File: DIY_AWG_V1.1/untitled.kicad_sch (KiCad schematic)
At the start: 61 parts, among them U1 AMS1117-3.3, U2 ADP7118ARDZ-3.3-R7, U3 ADP7118ARDZ-3.3-R7, U4 TPS7A3301RGWR, U5 TPS7A4701RGWR, U6 TPS7A3301RGWR, U7 TPS7A4701RGWR

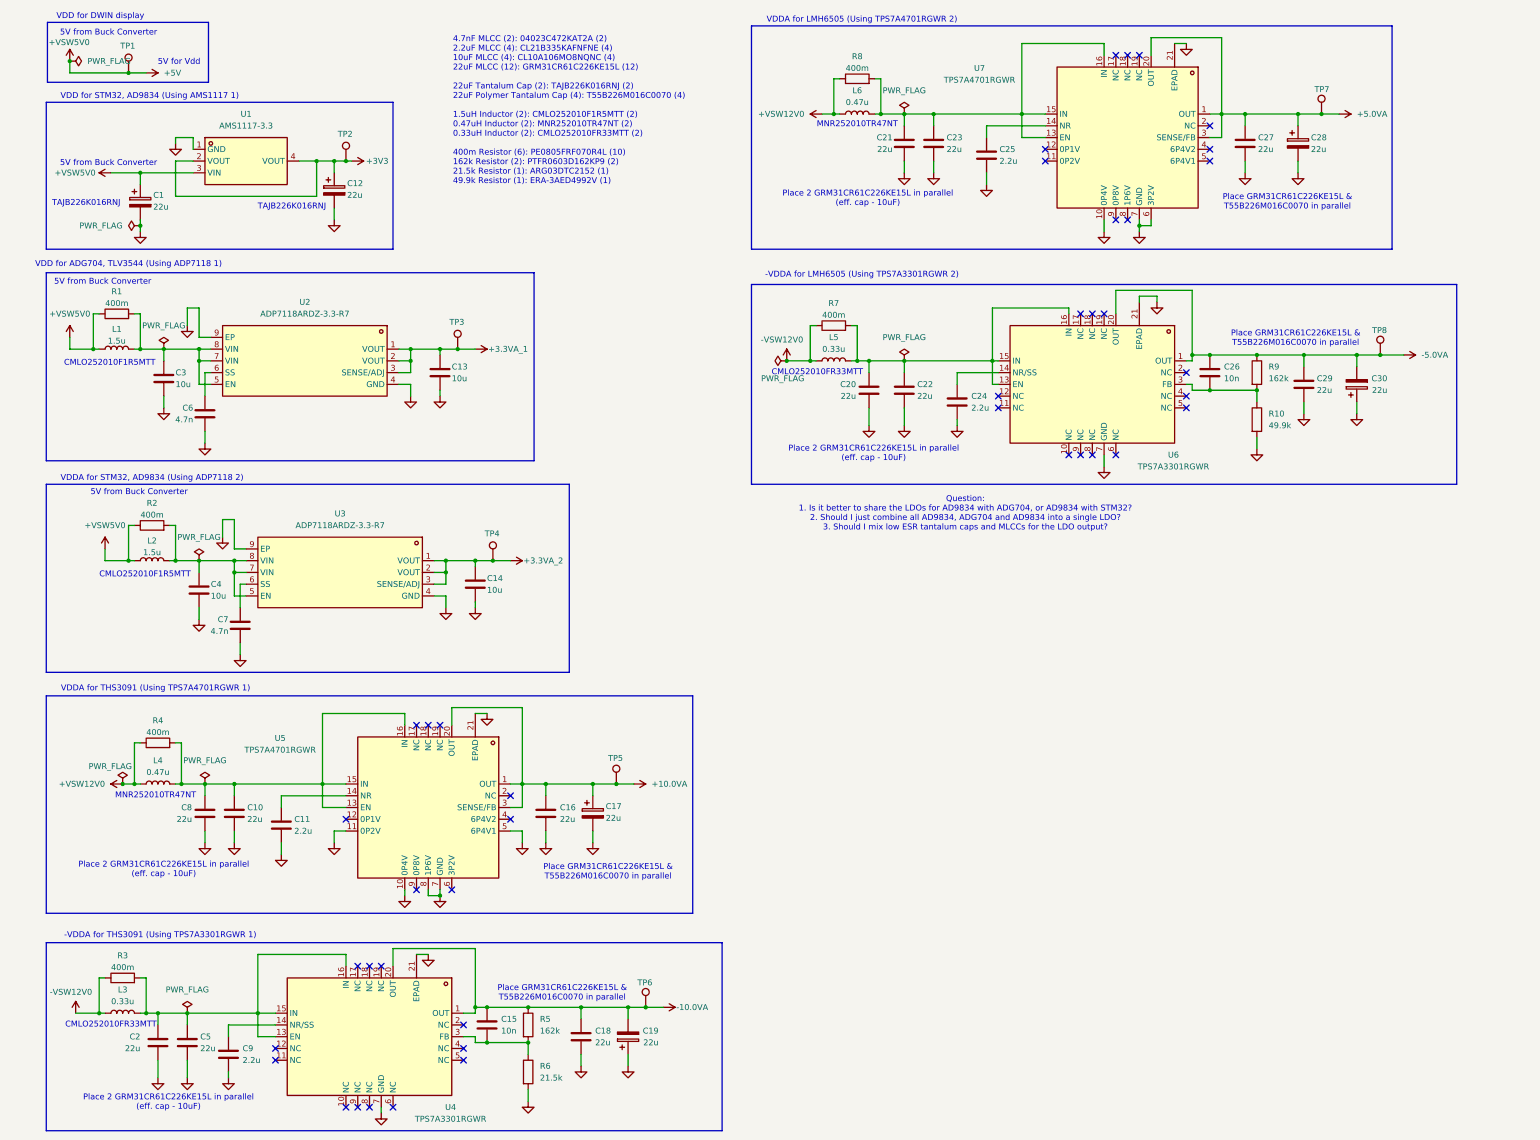
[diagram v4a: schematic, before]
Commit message: Updated component footprints
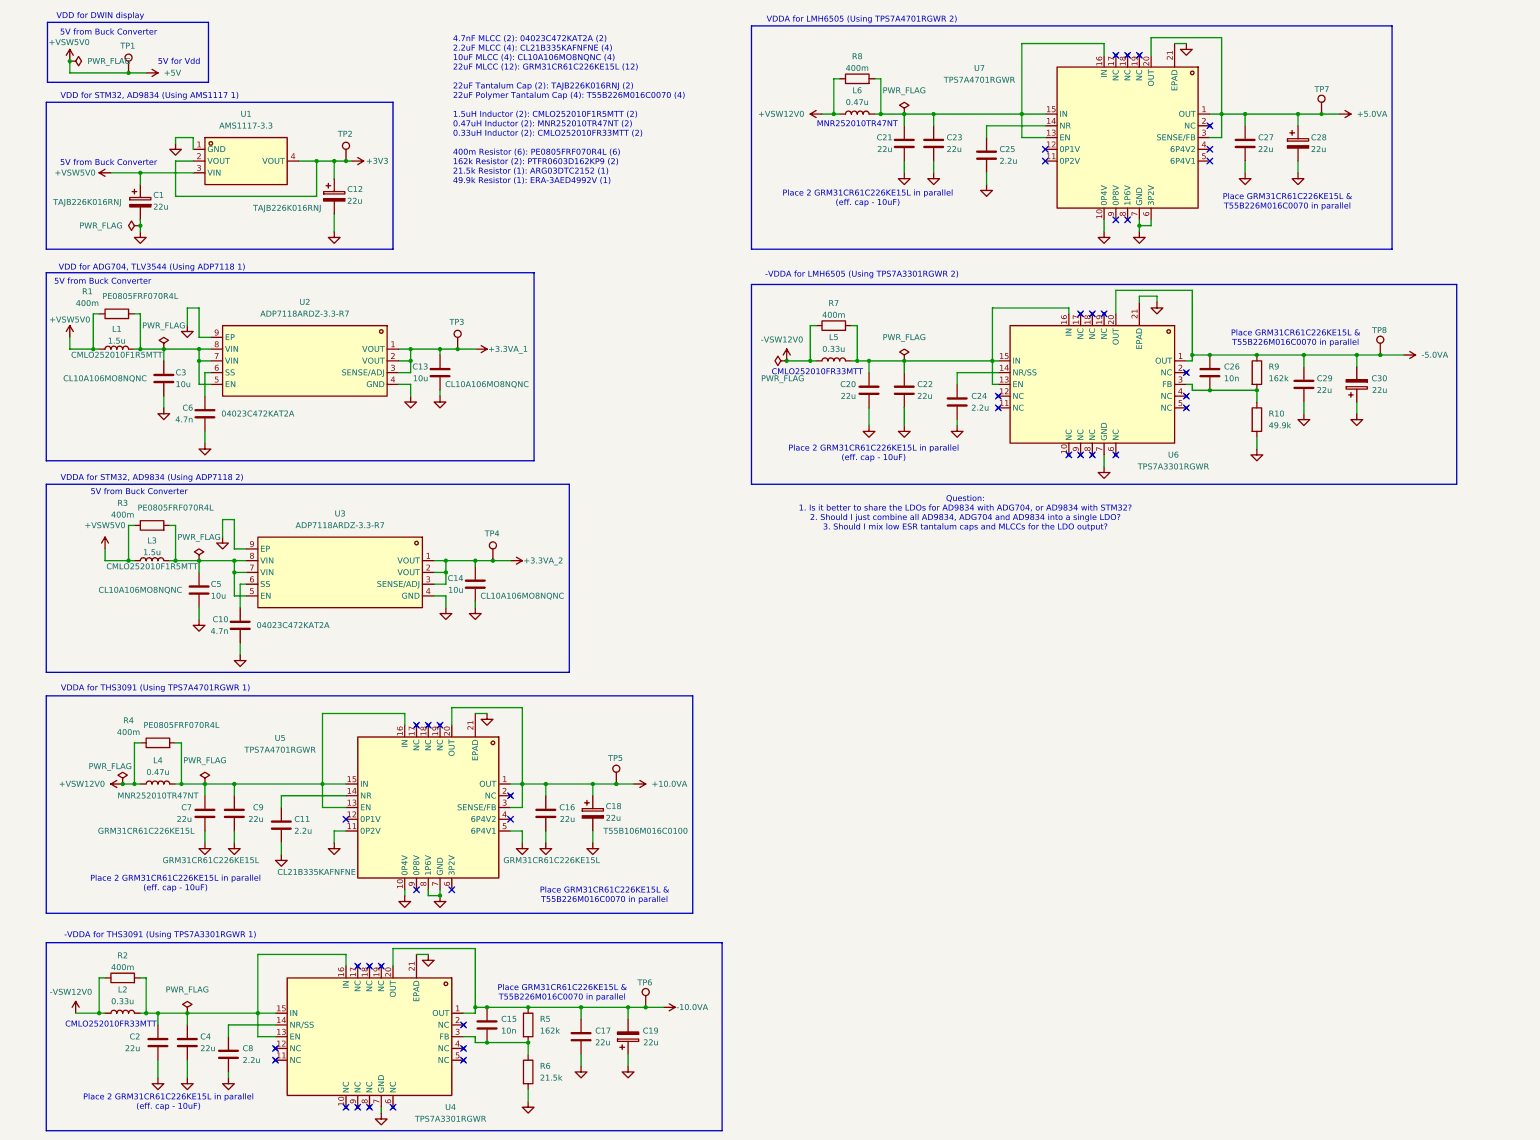
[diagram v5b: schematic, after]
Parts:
- removed C4: 10u, symbol Device:C
- removed C7: 4.7n, symbol Device:C
- removed L2: 1.5u, symbol Device:L
- removed R2: 400m, symbol Device:R
- added C5: 10u, Capacitor_SMD:C_0603_1608Metric, symbol Device:C
- added C9: 22u, Capacitor_SMD:C_1206_3216Metric, symbol Device:C
- added L3: 1.5u, Inductor_SMD:L_1008_2520Metric, symbol Device:L
- added R3: 400m, Resistor_SMD:R_0805_2012Metric, symbol Device:R
- C1: footprint (none) -> easyeda2kicad:CASE-B_3528; Component Name (none) -> TAJB226K016RNJ; LCSC ID: (none) -> C8020
- C10: value 22u -> 4.7n; footprint (none) -> Capacitor_SMD:C_0402_1005Metric; Component Name (none) -> 04023C472KAT2A
- C11: footprint (none) -> Capacitor_SMD:C_0805_2012Metric; Component Name (none) -> CL21B335KAFNFNE; LCSC ID (none) -> C16194987
- C12: footprint (none) -> easyeda2kicad:CASE-B_3528; Field6 (none) -> C8020; Name (none) -> TAJB226K016RNJ
- C13, C14, C3: footprint (none) -> Capacitor_SMD:C_0603_1608Metric; Component Name (none) -> CL10A106MO8NQNC; LCSC ID (none) -> C92487
- C16: footprint (none) -> Capacitor_SMD:C_1206_3216Metric; Component Name (none) -> GRM31CR61C226KE15L; LCSC ID (none) -> C77088
- C18: renamed from C17; footprint (none) -> easyeda2kicad:CAP-SMD_L3.5-W2.8-FD; Component Name (none) -> T55B106M016C0100; LCSC ID (none) -> C2158234
- C6: footprint (none) -> Capacitor_SMD:C_0402_1005Metric; Component Name (none) -> 04023C472KAT2A
- C7: renamed from C8; footprint (none) -> Capacitor_SMD:C_1206_3216Metric; Component Name (none) -> GRM31CR61C226KE15L; LCSC ID (none) -> C77088
- L1: footprint (none) -> Inductor_SMD:L_1008_2520Metric; Component Name (none) -> CMLO252010F1R5MTT; LCSC ID (none) -> C438917
- L4: footprint (none) -> Inductor_SMD:L_1008_2520Metric; Component Name (none) -> MNR252010TR47NT; LCSC ID (none) -> C18221969
- R1, R4: footprint (none) -> Resistor_SMD:R_0805_2012Metric; Component Name (none) -> PE0805FRF070R4L; LCSC ID (none) -> C7261230
- renumbered C18 to C17, C5 to C4, C9 to C8, L3 to L2, R3 to R2
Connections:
- net +5V: now also L3.1, R3.1
- net GND: now also C5.2, C9.2
- net at U3.5 (EN), U3.7 (VIN), U3.8 (VIN): now also C5.1, L3.2, R3.2
- net at U3.6 (SS): now also C10.1
- net at C7.1, L4.2, R4.2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: now also C9.1; no longer C10.1
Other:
- note removed: "CMLO252010F1R5MTT"
- note removed: "TAJB226K016RNJ"
- moved on the sheet: C12

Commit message: Updated component footprints
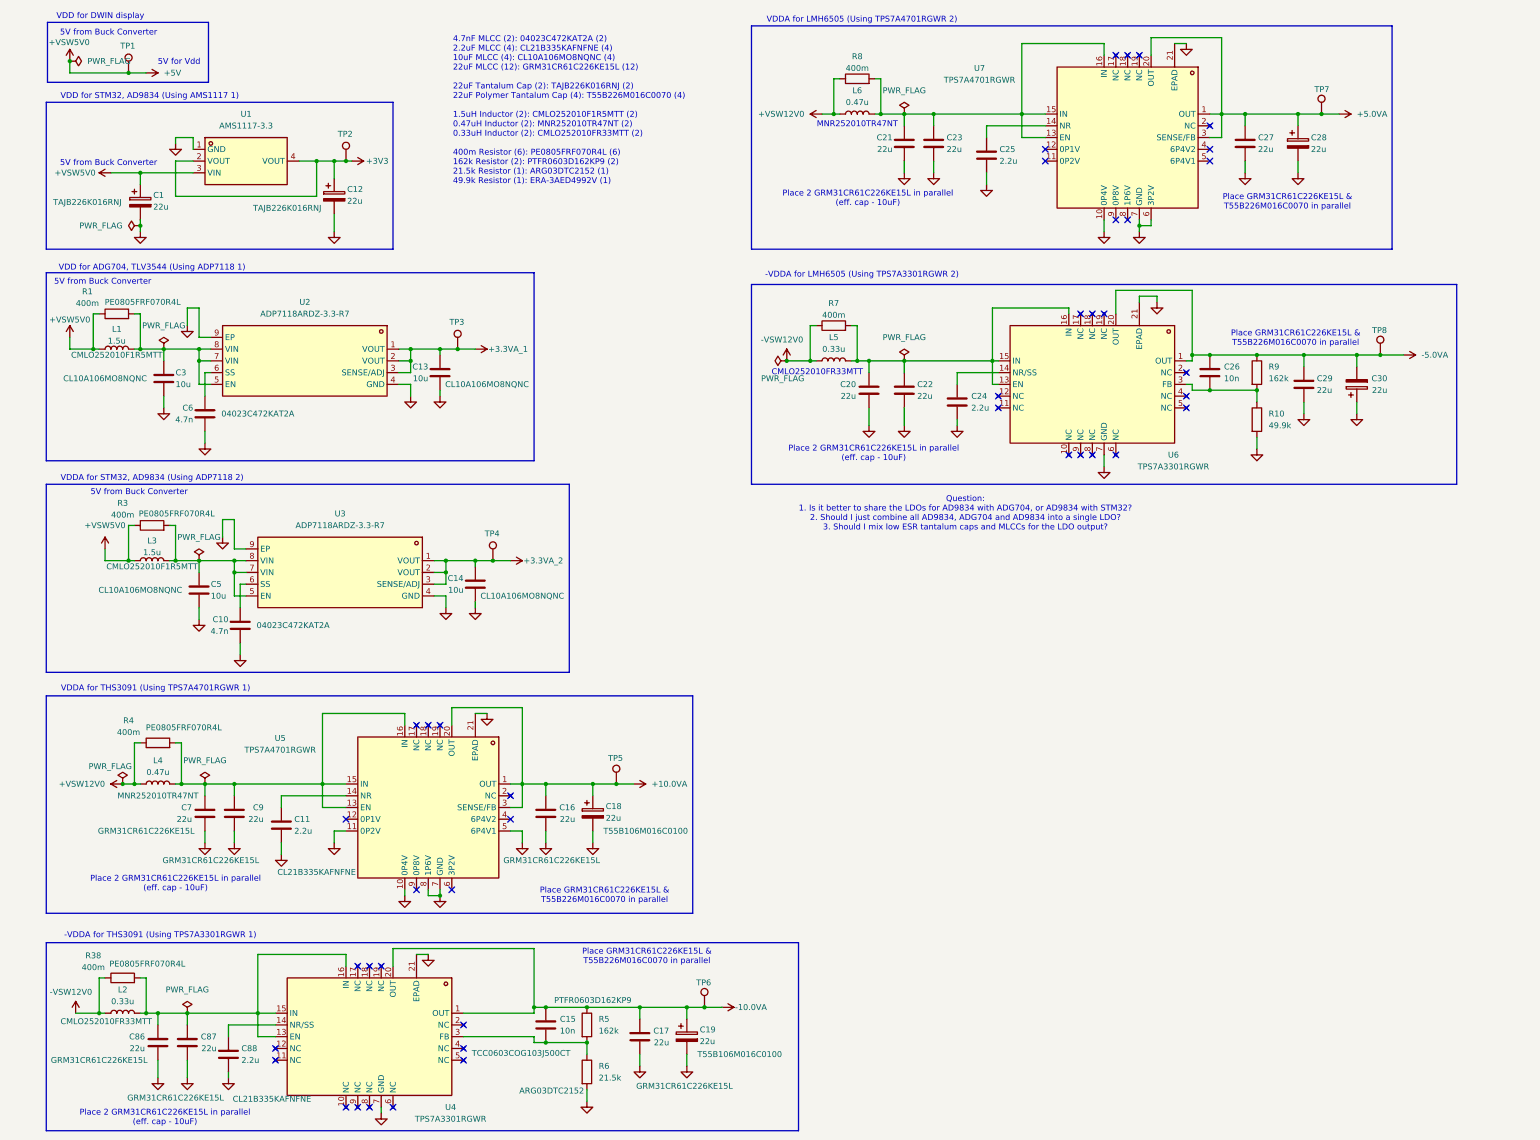
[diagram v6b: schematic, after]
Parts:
- removed C2, C4: 22u, symbol Device:C
- removed C8: 2.2u, symbol Device:C
- removed R2: 400m, symbol Device:R
- added C86, C87: 22u, Capacitor_SMD:C_1206_3216Metric, symbol Device:C
- added C88: 2.2u, Capacitor_SMD:C_0805_2012Metric, symbol Device:C
- added R38: 400m, Resistor_SMD:R_0805_2012Metric, symbol Device:R
- C15: footprint (none) -> Capacitor_SMD:C_0603_1608Metric; Component Name (none) -> TCC0603COG103J500CT; LCSC ID (none) -> C7393880
- C17: footprint (none) -> Capacitor_SMD:C_1206_3216Metric; Component Name (none) -> GRM31CR61C226KE15L; LCSC ID (none) -> C77088
- C19: footprint (none) -> easyeda2kicad:CAP-SMD_L3.5-W2.8-FD; Component Name (none) -> T55B106M016C0100; LCSC ID (none) -> C2158234
- L2: footprint (none) -> Inductor_SMD:L_1008_2520Metric; Component Name (none) -> CMLO252010FR33MTT; LCSC ID (none) -> C438913
- R5: footprint (none) -> Resistor_SMD:R_0603_1608Metric; Component Name (none) -> PTFR0603D162KP9; LCSC ID (none) -> C47116096
- R6: footprint (none) -> Resistor_SMD:R_0603_1608Metric; Component Name (none) -> ARG03DTC2152; LCSC ID (none) -> C311891
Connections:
- net -10.0VA: now also C19.1; no longer C19.2
- net -VSW12V0: now also R38.1
- net GND: now also C19.2, C86.2, C87.2, C88.2; no longer C19.1
- net at L2.2, U4.13 (EN), U4.15 (IN)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: now also C86.1, C87.1, R38.2
- net at U4.14 (NR/SS): now also C88.1
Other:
- moved on the sheet: C15, R5, R6, TP6

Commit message: Updated component footprints
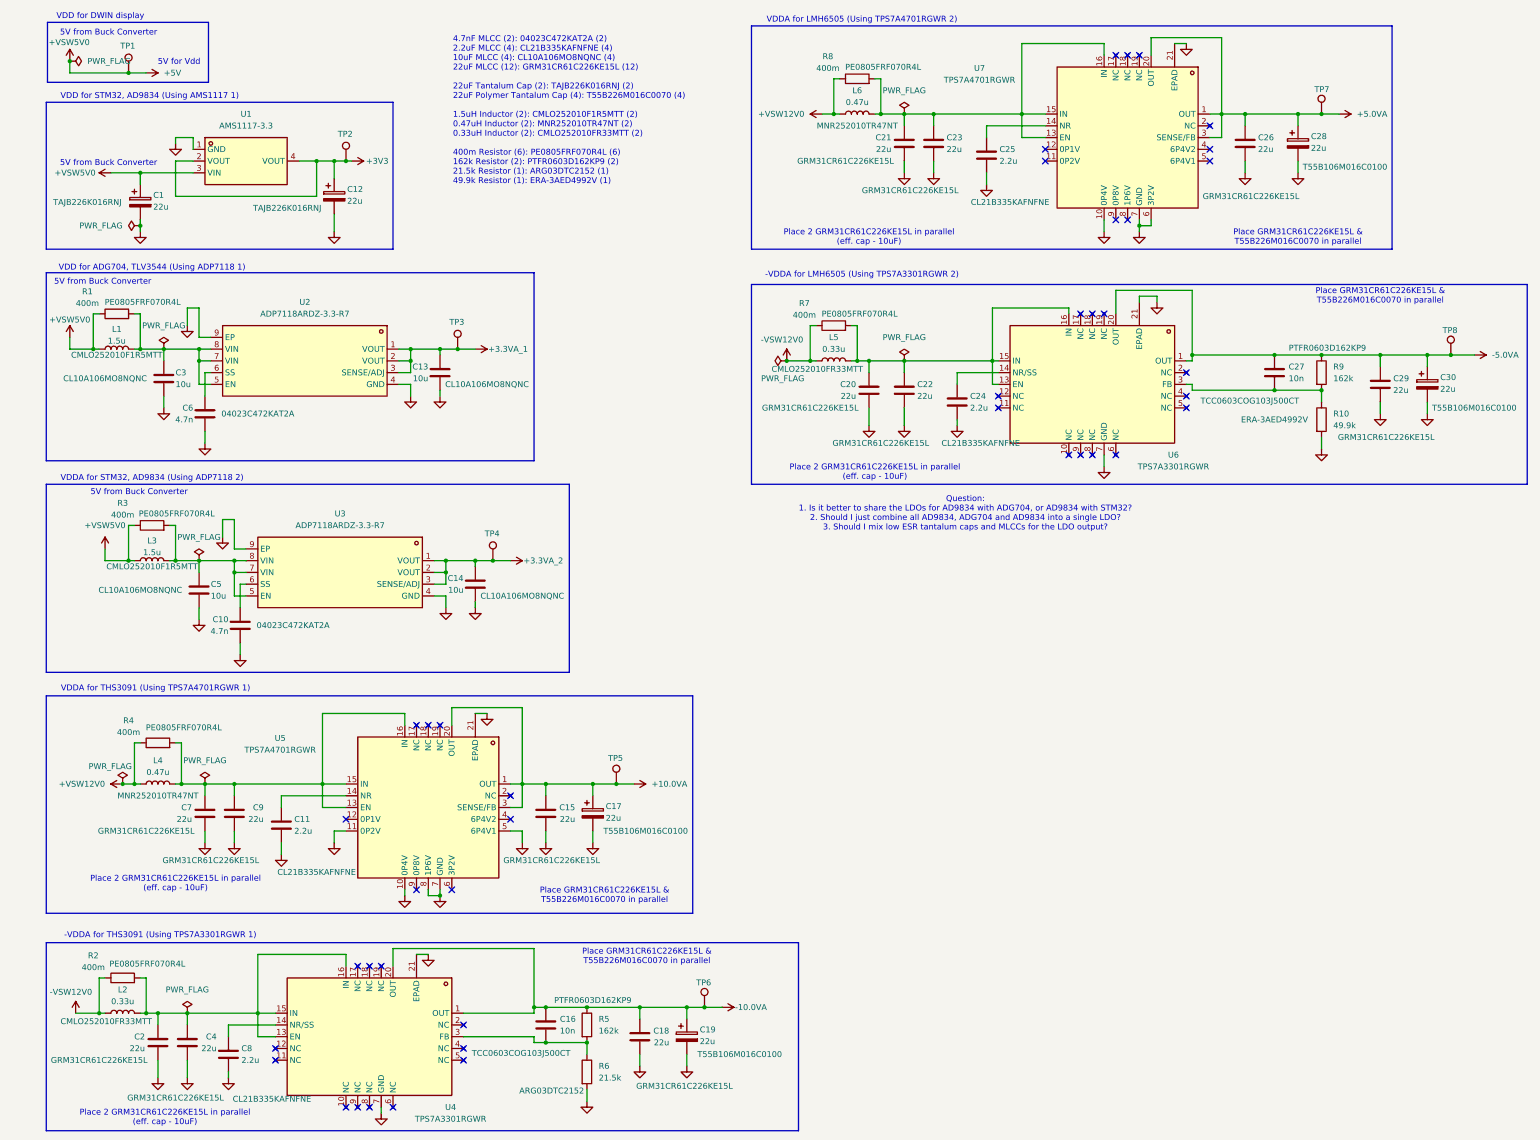
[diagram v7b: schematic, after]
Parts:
- C20, C21, C22, C23, C29: footprint (none) -> Capacitor_SMD:C_1206_3216Metric; Component Name (none) -> GRM31CR61C226KE15L; LCSC ID (none) -> C77088
- C24, C25: footprint (none) -> Capacitor_SMD:C_0805_2012Metric; Component Name (none) -> CL21B335KAFNFNE; LCSC ID (none) -> C16194987
- C26: value 10n -> 22u; footprint (none) -> Capacitor_SMD:C_1206_3216Metric; Component Name (none) -> GRM31CR61C226KE15L; LCSC ID (none) -> C77088
- C27: value 22u -> 10n; footprint (none) -> Capacitor_SMD:C_0603_1608Metric; Component Name (none) -> TCC0603COG103J500CT; LCSC ID (none) -> C7393880
- C28, C30: footprint (none) -> easyeda2kicad:CAP-SMD_L3.5-W2.8-FD; Component Name (none) -> T55B106M016C0100; LCSC ID (none) -> C2158234
- L5: footprint (none) -> Inductor_SMD:L_1008_2520Metric; Component Name (none) -> CMLO252010FR33MTT; LCSC ID (none) -> C438913
- L6: footprint (none) -> Inductor_SMD:L_1008_2520Metric; Component Name (none) -> MNR252010TR47NT; LCSC ID (none) -> C18221969
- R10: footprint (none) -> Resistor_SMD:R_0603_1608Metric; Component Name (none) -> ERA-3AED4992V; LCSC ID (none) -> C2074281
- R7, R8: footprint (none) -> Resistor_SMD:R_0805_2012Metric; Component Name (none) -> PE0805FRF070R4L; LCSC ID (none) -> C7261230
- R9: footprint (none) -> Resistor_SMD:R_0603_1608Metric; Component Name (none) -> PTFR0603D162KP9; LCSC ID (none) -> C47116096
- renumbered C16 to C15, C15 to C16, C18 to C17, C17 to C18, C86 to C2, C87 to C4, C88 to C8, R38 to R2
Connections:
- net +5.0VA: now also C26.1; no longer C27.1
- net -5.0VA: now also C27.1, C30.1; no longer C26.1, C30.2
- net GND: now also C26.2, C30.2; no longer C27.2, C30.1
- net at R10.1, R9.2, U6.3 (FB): now also C27.2; no longer C26.2
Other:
- note removed: "CMLO252010FR33MTT"
- note removed: "MNR252010TR47NT"
- moved on the sheet: R10, TP8
